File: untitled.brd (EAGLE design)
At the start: 94 x 50 mm, 65 parts, among them IC1 SIM68R, IC2 ST1S10PHR, IC3 BQ24072, IC4 SIM900, IC5 SMF05C, X1 ST-SMB-H, X2 ST-SMB-H

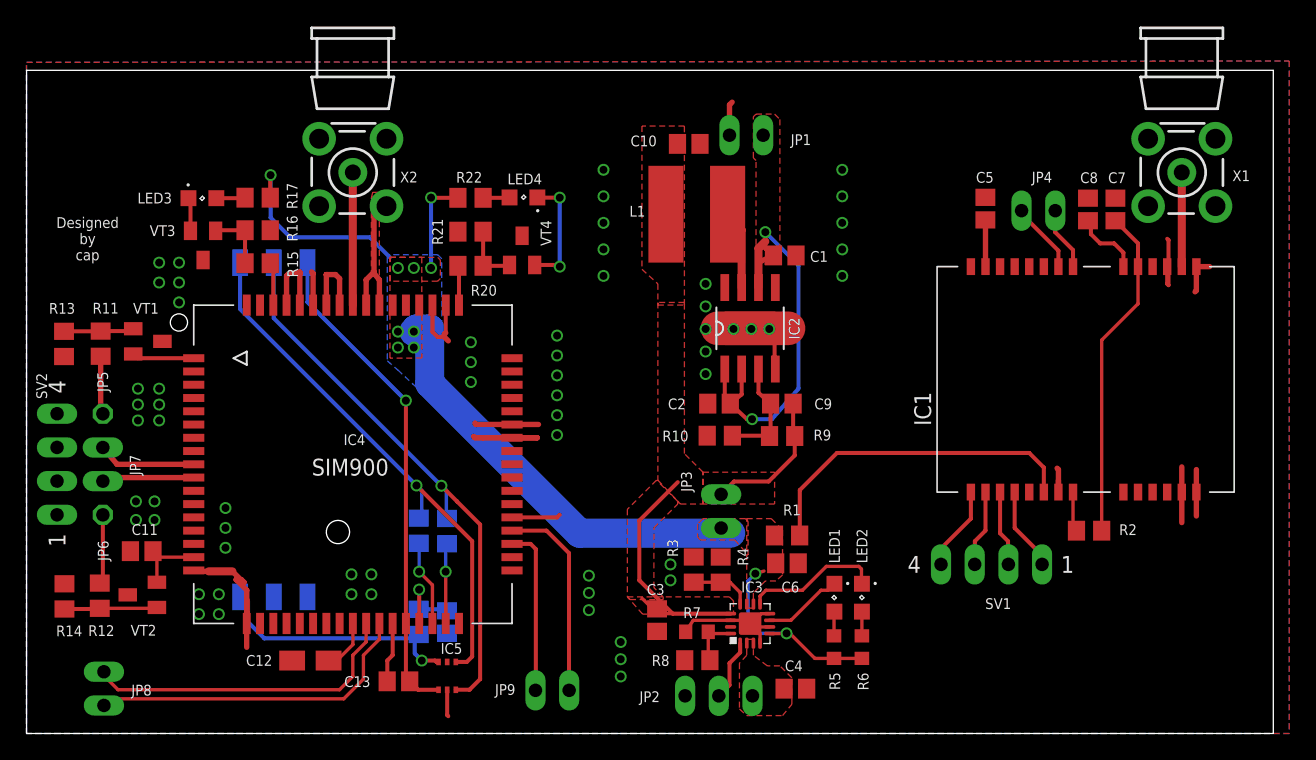
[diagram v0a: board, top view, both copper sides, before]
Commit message: New revision
Power supply moved to the top.
IO consolidated
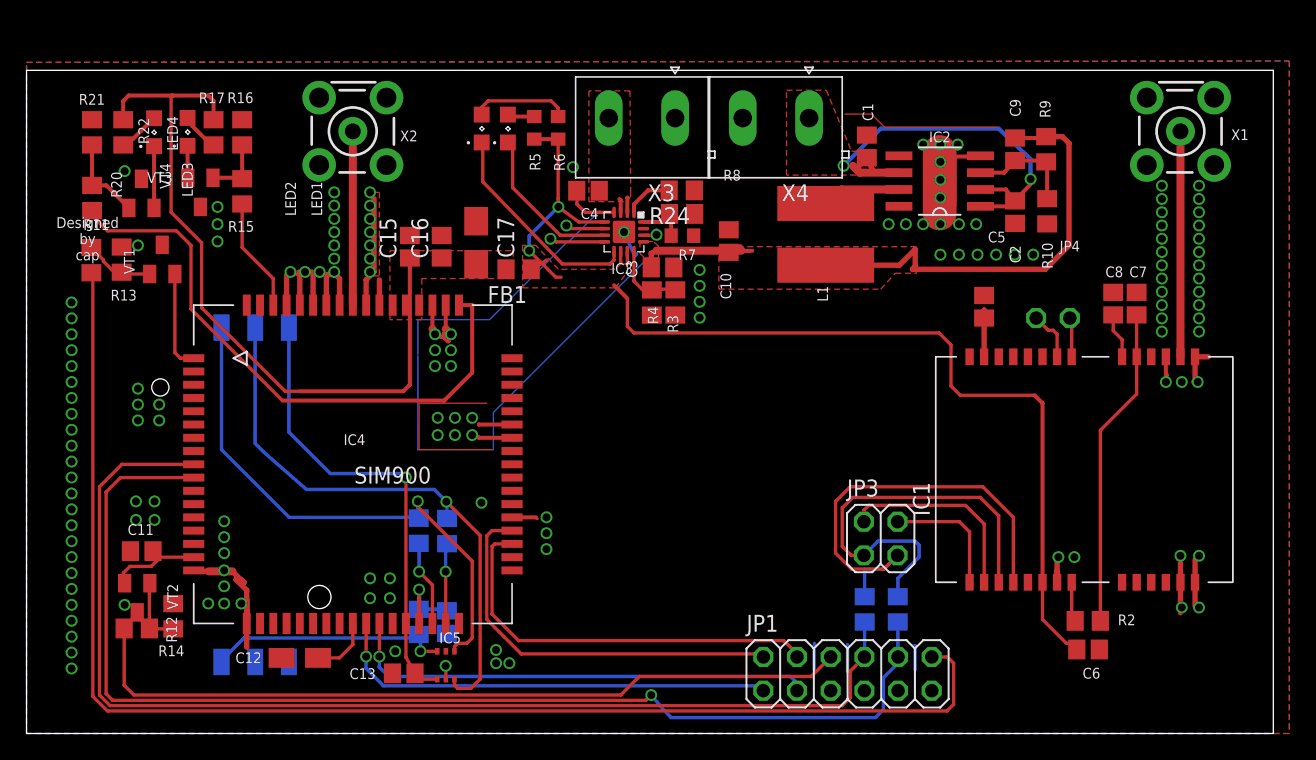
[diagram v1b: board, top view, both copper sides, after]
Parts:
- removed JP2: (no value), pinhead:1X03
- removed JP5, JP6: (no value), pinhead:1X01
- removed JP7, JP8, JP9: (no value), pinhead:1X02
- removed SV1, SV2: (no value), con-lstb:MA04-1
- added C15: 22p C0G, resistor:C0805
- added C16: 47p C0G, resistor:C0805
- added C17: 100u, rcl:B/3528-21W
- added FB1: BLM21PG221SN1D, murata-ferrite:R0805
- added R24: 10k, rcl:R0805
- added R25: 0, rcl:R0805
- added X3, X4: DG3XX-02-5.0, degson:DG306-5.0-02P
- C14: value 18p -> 22p
- JP1: device pinhead:1X02 -> pinhead:2X06
- JP3: device pinhead:1X02 -> pinhead:2X02
- JP4: device pinhead:1X02 -> pinhead:1X02ROUND
- R1: value 33 -> 0
- moved LED2 45.5 mm to (34.3, 45.6), turned to 90 degrees
- moved R6 45.4 mm to (40.1, 45.7)
- moved R5 45.2 mm to (38.3, 45.7)
- moved LED1 43.1 mm to (36.3, 45.6), turned to 90 degrees
- moved JP1 41.3 mm to (61.9, 4.50), flipped to the top, turned to 0 degrees
- moved C4 40.7 mm to (42.3, 40.9), turned to 180 degrees
- moved R8 33.7 mm to (49.4, 39.2), turned to 180 degrees
- moved IC3 31.0 mm to (45.0, 37.8), turned to 270 degrees
- moved R10 29.9 mm to (76.9, 39.4), turned to 90 degrees
- moved R7 29.9 mm to (49.5, 37.5), turned to 180 degrees
- moved R21 29.5 mm to (4.93, 45.3), turned to 270 degrees
- moved R9 29.4 mm to (76.9, 44.0), turned to 90 degrees
- moved VT4 29.0 mm to (8.66, 40.7)
- moved R20 29.0 mm to (4.94, 40.4), turned to 270 degrees
- moved LED4 28.3 mm to (9.62, 45.3), turned to 90 degrees
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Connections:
- removed net N$21: IC1.6, R1.1
- removed net N$28: IC1.4, SV1.1
- removed net N$29: IC1.3, SV1.2
- removed net N$33: IC4.38, JP9.1
- removed net N$34: IC4.37, JP9.2
- new net GPS_RXD: IC1.4, JP3.3, R25.1
- new net GPS_TXD: IC1.3, JP3.1, R1.1
- new net SIM_SCL: IC4.38, JP1.2
- new net SIM_SDA: IC4.37, JP1.4
- new net VBQ: C6.1, FB1.1, IC1.6, IC3.10, IC3.11, IC3.5, R5.1, R6.2
- net +12V: now also X4.1; no longer JP1.2
- net +4.8V: no longer JP3.1
- net BAT: now also X3.2; no longer JP2.3
- net DBG_RXD: now also JP1.3; no longer JP8.2
- net DBG_TXD: now also JP1.1; no longer JP8.1
- net GND: now also C15.2, C16.2, C17.-, JP1.11, JP1.5, JP1.7, JP1.9, R24.1, X3.1, X4.2; no longer JP1.1, JP2.1, SV2.1, SV2.2, SV2.3, SV2.4
- net N$30: now also JP3.2; no longer SV1.3
- net N$31: now also JP3.4; no longer SV1.4
- net POWER: now also JP1.12; no longer JP5.1
- net RESET: now also JP1.6; no longer JP6.1
- net RXD: now also JP1.10, R1.2; no longer JP7.2
- net TS: now also R24.2; no longer JP2.2
- net TXD: now also JP1.8, R25.2; no longer JP7.1
- net VBAT: now also C15.1, C16.1, C17.+, FB1.2; no longer C6.1, IC3.10, IC3.11, IC3.5, JP3.2, R1.2, R5.1, R6.2
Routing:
- net POWER: track 4.47 -> 103.8 mm
- net RXD: track 7.06 -> 89.4 mm, vias 0 -> 1
- net VBQ: track 0.00 -> 80.2 mm, vias 0 -> 2
- net TXD: track 7.44 -> 86.9 mm
- net RESET: track 5.24 -> 59.0 mm
- net N$20: track 3.00 -> 44.6 mm
- net GPS_RXD: track 0.00 -> 34.2 mm
- net GPS_TXD: track 0.00 -> 31.8 mm
- net N$51: track 0.00 -> 31.6 mm
- net SIM_SDA: track 0.00 -> 31.2 mm
- net SIM_SCL: track 0.00 -> 30.4 mm
- net N$21: track 25.3 -> 0.00 mm
- net VBAT: track 77.5 -> 55.2 mm, vias 11 -> 0
- net N$49: track 0.00 -> 19.7 mm
- net N$33: track 15.3 -> 0.00 mm
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- added copper zone on layer 1, net VBQ
- removed copper zone on layer 16, net VBAT

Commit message: Production ready version
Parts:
- removed JP3: (no value), pinhead:2X02
- JP1: device pinhead:2X06 -> pinhead:2X09
- moved C10 12.7 mm to (65.6, 37.0)
- moved JP1 7.60 mm to (54.3, 4.40)
- moved R1 6.88 mm to (58.9, 8.51), turned to 0 degrees
- moved R25 4.50 mm to (58.9, 10.6), turned to 0 degrees
- moved R12 2.33 mm to (7.11, 5.92)
- moved C11 2.19 mm to (7.08, 12.2)
- moved VT2 2.00 mm to (6.75, 9.03)
- moved R14 1.36 mm to (9.76, 9.24)
- moved R3 0.45 mm to (46.9, 32.1)
- moved R4 0.41 mm to (49.0, 32.1)
- moved FB1 0.36 mm to (37.4, 35.2)
- moved C8 0.30 mm to (81.6, 32.4)
- moved R5 0.30 mm to (38.0, 45.7)
- moved VT4 0.20 mm to (8.87, 40.7)
- moved LED4 0.20 mm to (9.81, 45.3)
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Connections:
- removed net N$30: IC1.2, JP3.2
- removed net N$31: IC1.1, JP3.4
- new net GPS_SCL: IC1.2, JP1.17
- new net GPS_SDA: IC1.1, JP1.15
- new net VDD_EXT: IC4.15, JP1.14
- net GND: now also JP1.13
- net GPS_RXD: now also JP1.18; no longer JP3.3
- net GPS_TXD: now also JP1.16; no longer JP3.1
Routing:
- net VDD_EXT: track 0.00 -> 76.4 mm
- net N$51: track 31.6 -> 0.00 mm
- net RXD: track 89.4 -> 65.1 mm
- net N$49: track 19.7 -> 0.00 mm
- net TXD: track 86.9 -> 67.5 mm, vias 0 -> 1
- net GPS_SDA: track 0.00 -> 16.5 mm
- net GND: track 94.5 -> 78.4 mm, vias 149 -> 166
- net SIM_SCL: track 30.4 -> 15.1 mm, vias 0 -> 1
- net N$30: track 15.1 -> 0.00 mm
- net GPS_SCL: track 0.00 -> 15.0 mm
- net SIM_SDA: track 31.2 -> 16.2 mm, vias 0 -> 1
- net N$50: track 14.1 -> 0.00 mm
- net N$47: track 11.9 -> 0.00 mm
- net DBG_RXD: track 35.9 -> 25.2 mm
- net DBG_TXD: track 34.0 -> 23.7 mm
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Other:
- board text added: "2.8 V"
- board text added: "GND"
- board text added: "POWER"
- board text added: "RESET"
- board text added: "RXD"
- board text added: "RX_GPS"
- board text added: "RX_GSM"
- board text added: "SCL"
- board text added: "SCL_GSM"
- board text added: "SDA"
- board text added: "SDA_GSM"
- board text added: "TXD"
- board text added: "TX_GPS"
- board text added: "TX_GSM"

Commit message: Ready for production
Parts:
- moved R8 1.92 mm to (51.2, 39.8), turned to 270 degrees
- moved R3 1.72 mm to (48.0, 30.7), turned to 180 degrees
- moved R7 1.58 mm to (48.7, 38.8)
- moved R24 1.25 mm to (48.1, 40.9)
- moved R4 1.24 mm to (48.0, 32.8), turned to 180 degrees
- moved C3 0.30 mm to (48.0, 34.8)
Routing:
- net N$5: track 3.93 -> 6.26 mm
- net TS: track 3.70 -> 2.52 mm
- net VBQ: track 79.6 -> 80.6 mm
- net GND: vias 166 -> 173
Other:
- board text added: "Designed by Ivan Pylypenko"
- board text removed: "Designed by cap"
